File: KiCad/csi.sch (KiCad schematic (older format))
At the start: 38 parts, among them IC1 TCA9548ARGER, J6 WE_68715014522, J7 WE_68715014022

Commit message: Update comments, move things around on PCB
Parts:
- removed IC1: TCA9548ARGER, jetson-nano-baseboard-footprints:VQFN-24, symbol jetson-nano-baseboard:TCA9548A
- removed R39: R_0R_0402, jetson-nano-baseboard-footprints:0402-res, symbol jetson-nano-baseboard:R_0R_0402
- removed TP11, TP12: ~, jetson-nano-baseboard-footprints:TP-R-1.5, symbol jetson-nano-baseboard:Testpad
- added U3: PCA9544ABS, antmicro-footprints:VQFN-20-1EP_5x5mm, symbol antmicroLogicSignalSwitchesMultiplexersDecoders:PCA9544ABS
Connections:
- net labels removed: Texas Instruments
- wire segments 210 -> 205
- no-connect marks 40 -> 39
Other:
- note removed: "0b1110000R"
- note removed: "0x70h"
- note removed: "I2C address:"
- moved on the sheet: C9, R13, R15, R17, R19, R21, R34, R35, R57, R58, R59, R60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

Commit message: Move ethernet connector closet to the edge. Loclib
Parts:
- U3: footprint antmicro-footprints:VQFN-20-1EP_5x5mm -> jetson-nano-baseboard-footprints:VQFN-20-1EP_5x5mm; symbol antmicroLogicSignalSwitchesMultiplexersDecoders:PCA9544ABS -> jetson-nano-baseboard:PCA9544ABS
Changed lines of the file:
@@
 Camera I2C multiplexer
 $Comp
-L antmicroLogicSignalSwitchesMultiplexersDecoders:PCA9544ABS U3
+L jetson-nano-baseboard:PCA9544ABS U3
 U 1 1 625E77A9
 P 4150 9550
 F 0 "U3" H 4150 10393 60  0000 C CNN
 F 1 "PCA9544ABS" H 4150 8600 60  0001 C CNN
-F 2 "antmicro-footprints:VQFN-20-1EP_5x5mm" H 3850 8500 60  0001 L CNN
+F 2 "jetson-nano-baseboard-footprints:VQFN-20-1EP_5x5mm" H 3850 8500 60  0001 L CNN
 F 3 "https://www.nxp.com/docs/en/data-sheet/PCA9544A.pdf" H 4300 9200 60  0001 L CNN
 F 4 "PCA9544ABS,118" H 4150 10287 60  0000 C CNN "MPN"

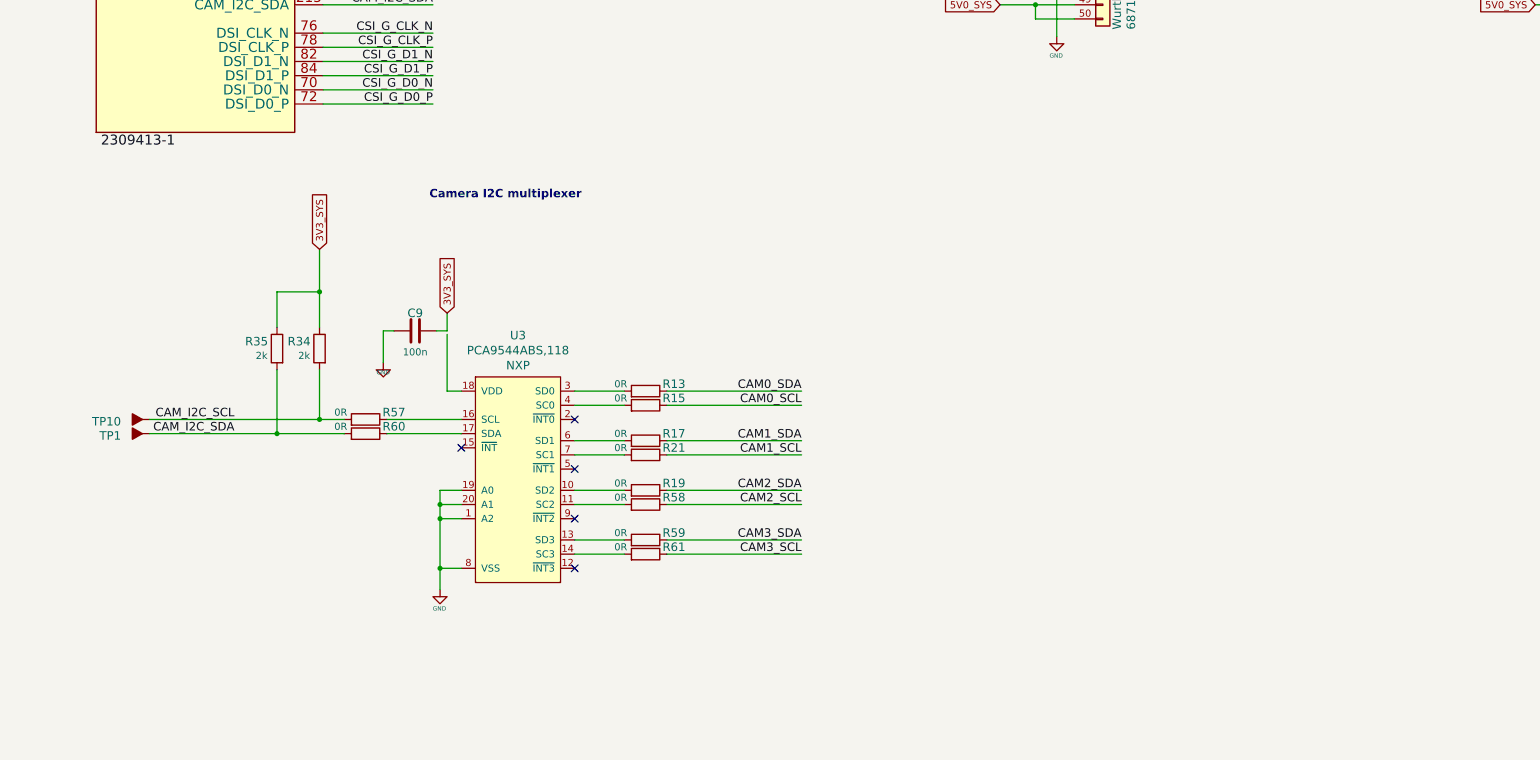
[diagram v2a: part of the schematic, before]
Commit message: Change I2C mux
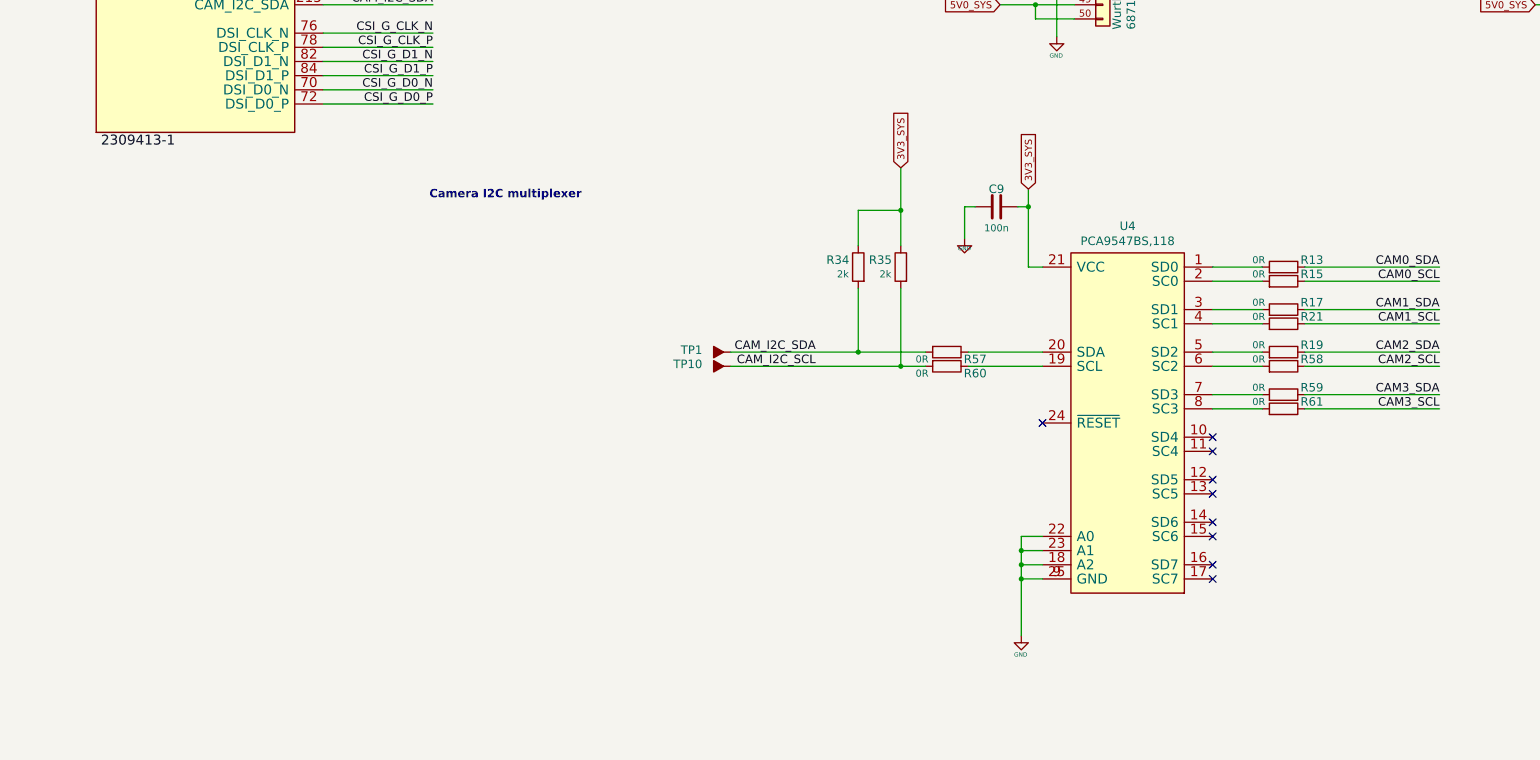
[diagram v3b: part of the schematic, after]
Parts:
- removed U3: PCA9544ABS, jetson-nano-baseboard-footprints:VQFN-20-1EP_5x5mm, symbol jetson-nano-baseboard:PCA9544ABS
- added U4: PCA9547BS,118, antmicro-footprints:HVQFN24, symbol antmicroLogicSignalSwitchesMultiplexersDecoders:PCA9547BS,118
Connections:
- net 3V3_SYS: now also U4.21 (VCC)
- net CAM_I2C_SCL: now also R35.2, R60.2; no longer R34.2, R57.2
- net CAM_I2C_SDA: now also R34.2, R57.2; no longer R35.2, R60.2
- net GND: now also U4.18 (A2), U4.22 (A0), U4.23 (A1), U4.25 (GND), U4.9 (GND)
- net at R13.2: now also U4.1 (SD0)
- net at R15.2: now also U4.2 (SC0)
- net at R17.2: now also U4.3 (SD1)
- net at R21.2: now also U4.4 (SC1)
- net at R19.2: now also U4.5 (SD2)
- net at R58.2: now also U4.6 (SC2)
- net at R59.2: now also U4.7 (SD3)
- net at R61.2: now also U4.8 (SC3)
- net at R57.1: now also U4.20 (SDA)
- net at R60.1: now also U4.19 (SCL)
- no-connect marks 39 -> 43
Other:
- moved on the sheet: C9, R13, R15, R17, R19, R21, R34, R35, R57, R58, R59, R60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

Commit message: Rework 3V3 and 5V DCDC on schematic, layout 3V3 DCDC
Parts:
- U4: footprint antmicro-footprints:HVQFN24 -> jetson-nano-baseboard-footprints:HVQFN24; symbol antmicroLogicSignalSwitchesMultiplexersDecoders:PCA9547BS,118 -> jetson-nano-baseboard:PCA9547BS,118
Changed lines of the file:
@@
 	7375 7800 7300 7800
 $Comp
-L antmicroLogicSignalSwitchesMultiplexersDecoders:PCA9547BS,118 U4
+L jetson-nano-baseboard:PCA9547BS,118 U4
 U 1 1 61C7982E
 P 8450 9325
 F 0 "U4" H 8450 10714 60  0000 C CNN
 F 1 "PCA9547BS,118" H 8450 10608 60  0000 C CNN
-F 2 "antmicro-footprints:HVQFN24" H 8450 9325 60  0001 C CNN
+F 2 "jetson-nano-baseboard-footprints:HVQFN24" H 8450 9325 60  0001 C CNN
 F 3 "https://pl.mouser.com/datasheet/2/302/PCA9547-1127544.pdf" H 8450 9325 60  0001 C CNN
 F 4 "Nexperia" H 8450 9325 50  0001 C CNN "Manufacturer"
